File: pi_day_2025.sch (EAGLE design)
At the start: 109 parts, among them IC1 W25Q64JVXGIQ, J4 SM03B-SRSS-TB(LF)(SN), Q2 310mA/60V/1.6Ω, U1 APS6404L-3SQR-ZR, U2 RP2350A, U3 TPS76318DBVRG4, U4 TPS63001DRCR, U5 TXS0108EPWRG4, U6 LSM6DS3TR-C, U7 MCP73833T-AMI/MF, U8 TPS2113APWR, U9 ESP32-C3-MINI-1-N4, Y1 12MHz

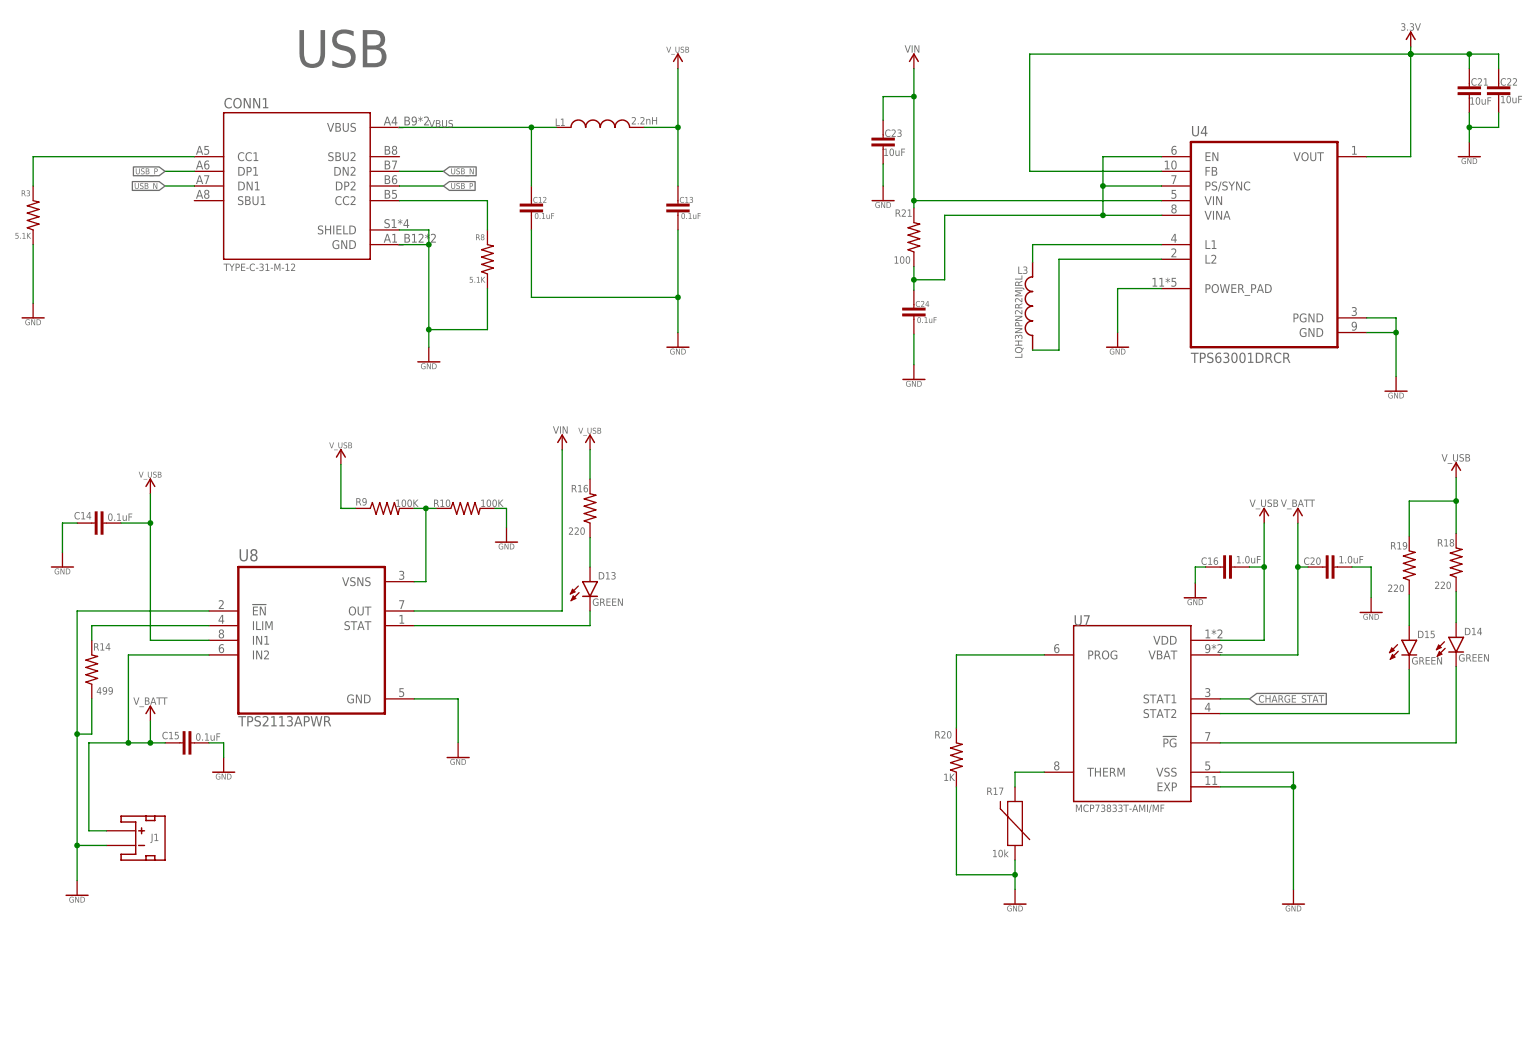
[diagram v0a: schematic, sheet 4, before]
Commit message: Added voltage symbols
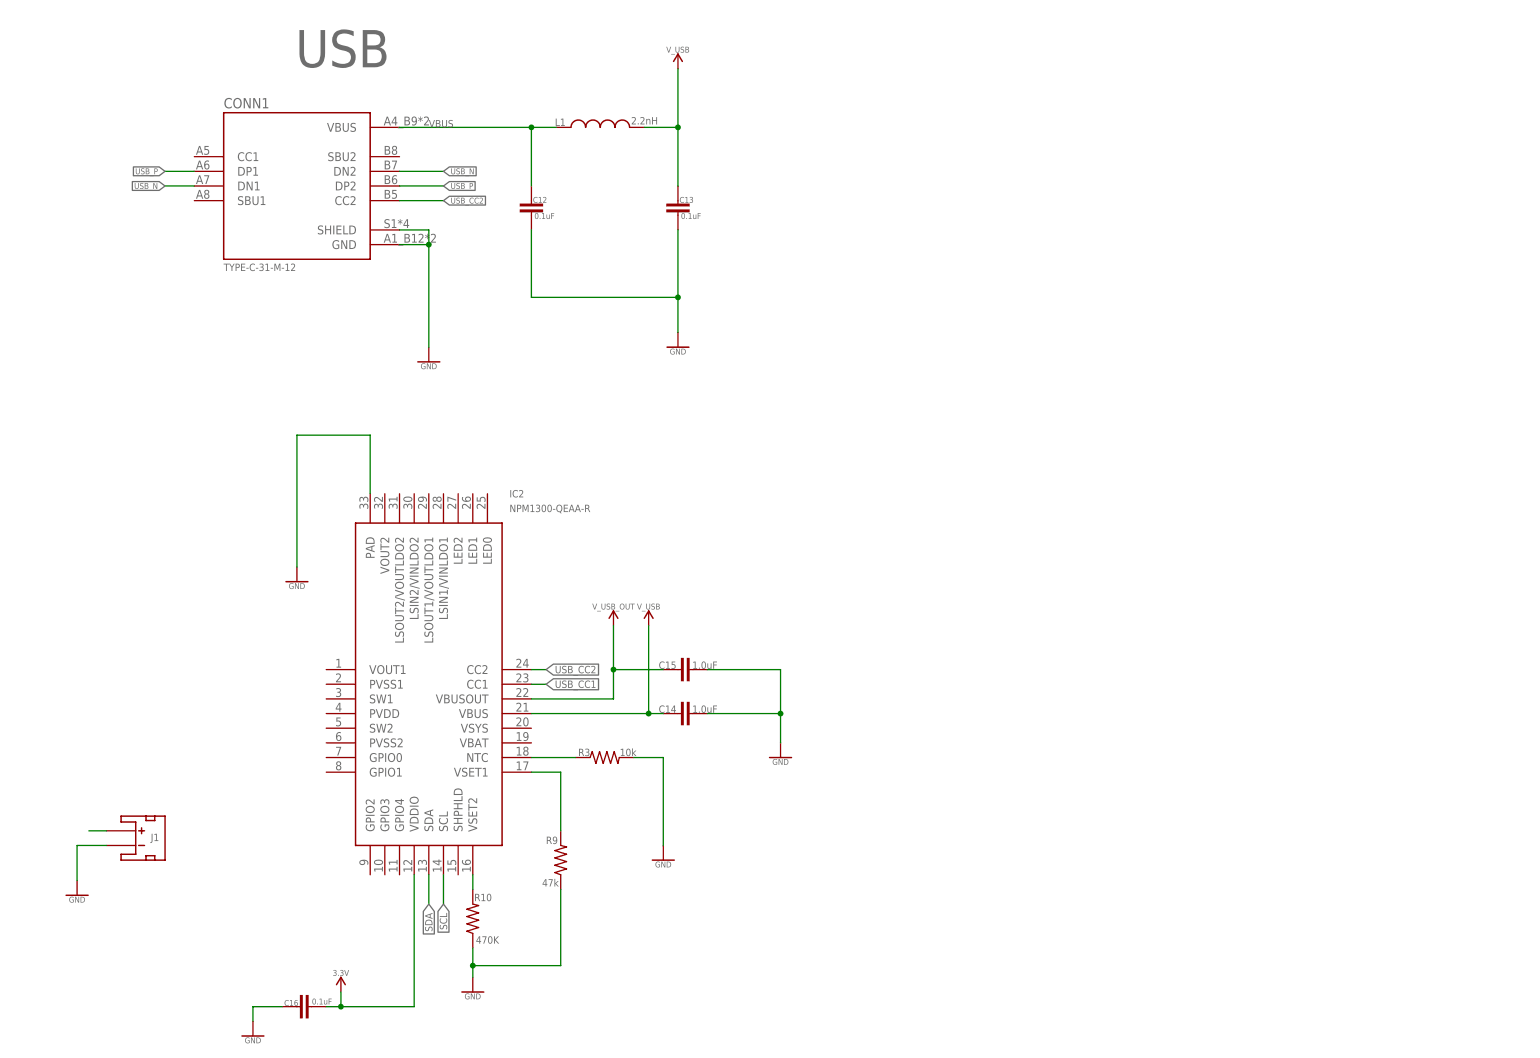
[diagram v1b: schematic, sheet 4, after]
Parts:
- removed C20, C26: 1.0uF, SparkFun-Capacitors:1.0UF-0402-16V-10%
- removed C21, C22, C23: 10uF, SparkFun-Capacitors:10UF-0402T-6.3V-20%
- removed C24: 0.1uF, SparkFun-Capacitors:0.1UF-0402-16V-10%
- removed C25: 4.7uF, SparkFun-Capacitors:4.7UF-0402_TIGHT-6.3V-20%-X5R
- removed D13, D14, D15: GREEN, SparkFun-LED:LED-GREEN0603
- removed L3: LQH3NPN2R2MJRL, LQH3NPN2R2MJRL:LQH3NPN2R2MJRL
- removed R14: 499, SparkFun-Resistors:RESISTOR0402
- removed R16, R18, R19: 220, SparkFun-Resistors:220OHM-0402-TIGHT-1/16W-1%
- removed R17: 10k, SparkFun-Resistors:NTC-THERMISTOR-0603
- removed R20: 1K, SparkFun-Resistors:1KOHM-0402-1/16W-1%
- removed R21: 100, SparkFun-Resistors:100OHM-0402-TIGHT-1/16W-1%
- removed R8: 5.1K, SparkFun-Resistors:RESISTOR0402
- removed U3: TPS76318DBVRG4, TPS76318DBVRG4:TPS76318DBVRG4
- removed U4: TPS63001DRCR, TPS63001DRCR:TPS63001DRCR
- removed U7: MCP73833T-AMI/MF, MCP73833T-AMI_MF:MCP73833T-AMI/MF
- removed U8: TPS2113APWR, TPS2113APWR:TPS2113APWR
- added IC2: NPM1300-QEAA-R, SamacSys_Parts:NPM1300-QEAA-R
- C14, C15: value 0.1uF -> 1.0uF; device SparkFun-Capacitors:0.1UF-0402-10V-10%-X7R -> SparkFun-Capacitors:1.0UF-0402-16V-10%
- C16: value 1.0uF -> 0.1uF; device SparkFun-Capacitors:1.0UF-0402-16V-10% -> SparkFun-Capacitors:0.1UF-0402-16V-10%
- R10: value 100K -> 470K; device SparkFun-Resistors:100KOHM-0402-1/16W-1% -> SparkFun-Resistors:RESISTOR0402
- R3: value 5.1K -> 10k; device SparkFun-Resistors:RESISTOR0402 -> SparkFun-Resistors:10KOHM-0402-1/16W-1%
- R4: value DNF -> (none)
- R5: value 1K -> (none)
- R6, R7: value 2.2K -> (none)
- R9: value 100K -> 47k; device SparkFun-Resistors:100KOHM-0402-1/16W-1% -> SparkFun-Resistors:47KOHM-0402-1/10W-1%
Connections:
- removed net N$10: D13.C, U8.STAT
- removed net N$14: R17.2, U7.THERM
- removed net N$15: D14.A, R18.1
- removed net N$16: D14.C, U7.!PG
- removed net N$17: D15.A, R19.1
- removed net N$18: D15.C, U7.STAT2
- removed net N$19: R20.2, U7.PROG
- removed net N$20: L3.P$2, U4.L1
- removed net N$21: L3.P$1, U4.L2
- removed net N$22: C24.1, R21.1, U4.EN, U4.PS/SYNC, U4.VINA
- removed net N$8: R14.2, U8.ILIM
- removed net N$9: D13.A, R16.1
- removed net VIN: C23.1, R21.2, U4.VIN, U8.OUT
- removed net V_BATT: C15.1, C20.1, J1.+, U7.VBAT, U8.IN2
- new net N$38: J1.+
- new net USB_CC1: IC2.CC1
- new net USB_CC2: CONN1.CC2, IC2.CC2
- net 1.8V: no longer C25.1, U3.OUT
- net 3.3V: now also C16.2, IC2.VDDIO; no longer C21.1, C22.1, C26.1, U3.EN, U3.IN, U4.FB, U4.VOUT
- net CHARGE_STAT: no longer U7.STAT1
- net GND: now also C14.2, IC2.PAD, R10.1, R3.2, R9.1; no longer C14.1, C20.2, C21.2, C22.2, C23.2, C24.2, C25.2, C26.2, R10.2, R14.1, R17.1, R20.1, R3.1, R8.1, U3.GND, U4.GND, U4.PGND, U4.POWER_PAD, U7.EXP, U7.VSS, U8.!EN, U8.GND
- net N$3: now also IC2.NTC, R3.1; no longer CONN1.CC1, R3.2
- net N$6: now also IC2.VSET2, R10.2; no longer R10.1, R9.2, U8.VSNS
- net N$7: now also IC2.VSET1, R9.2; no longer CONN1.CC2, R8.2
- net SCL: now also IC2.SCL
- net SDA: now also IC2.SDA
- net V_USB: now also C14.1, C15.1, IC2.VBUS, IC2.VBUSOUT; no longer C14.2, C16.2, R16.2, R18.2, R19.2, R9.1, U7.VDD, U8.IN1
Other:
- moved on the sheet: C14, C15, C16, R10, R3, R9

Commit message: more modification
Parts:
- added R8: 0, SparkFun-Resistors:0OHM-0603-1/10W
- R10: value 470K -> (none)
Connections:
- new net N$8: IC2.SHPHLD, R8.2
- net GND: now also R8.1
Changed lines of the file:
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@@
 <part name="GND22" library="SparkFun-PowerSymbols" library_urn="urn:adsk.eagle:library:530" deviceset="GND" device=""/>
 <part name="R9" library="SparkFun-Resistors" library_urn="urn:adsk.eagle:library:532" deviceset="47KOHM" device="-0402-1/10W-1%" package3d_urn="urn:adsk.eagle:package:41389023/1" value="47k"/>
-<part name="R10" library="SparkFun-Resistors" library_urn="urn:adsk.eagle:library:532" deviceset="RESISTOR" device="0402" package3d_urn="urn:adsk.eagle:package:39657/2" value="470K"/>
+<part name="R10" library="SparkFun-Resistors" library_urn="urn:adsk.eagle:library:532" deviceset="RESISTOR" device="0402" package3d_urn="urn:adsk.eagle:package:39657/2" value=" "/>
 <part name="C14" library="SparkFun-Capacitors" library_urn="urn:adsk.eagle:library:510" deviceset="1.0UF" device="-0402-16V-10%" package3d_urn="urn:adsk.eagle:package:41385089/1" value="1.0uF"/>
 <part name="GND23" library="SparkFun-PowerSymbols" library_urn="urn:adsk.eagle:library:530" deviceset="GND" device=""/>
@@
 <part name="C16" library="SparkFun-Capacitors" library_urn="urn:adsk.eagle:library:510" deviceset="0.1UF" device="-0402-16V-10%" package3d_urn="urn:adsk.eagle:package:41385089/1" override_package3d_urn="urn:adsk.eagle:package:44163394/2" override_package_urn="urn:adsk.eagle:footprint:37389/1" override_locally_modified="yes" value="0.1uF"/>
 <part name="GND26" library="SparkFun-PowerSymbols" library_urn="urn:adsk.eagle:library:530" deviceset="GND" device=""/>
+<part name="R8" library="SparkFun-Resistors" library_urn="urn:adsk.eagle:library:532" deviceset="0OHM" device="-0603-1/10W" package3d_urn="urn:adsk.eagle:package:41389018/1" value="0"/>
 </parts>
 <sheets>
@@
 <attribute name="VALUE" x="48.26" y="2.286" size="1.016" layer="96" font="vector" ratio="20" align="top-center"/>
 </instance>
+<instance part="R8" gate="G$1" x="83.82" y="22.098" smashed="yes" rot="R90">
+<attribute name="NAME" x="82.55" y="26.924" size="1.27" layer="95" font="vector" ratio="20" rot="R180" align="bottom-center"/>
+<attribute name="VALUE" x="83.058" y="17.272" size="1.27" layer="96" font="vector" ratio="20" rot="R180" align="top-center"/>
+</instance>
 </instances>
 <busses>
@@
 <junction x="86.36" y="14.732"/>
 <pinref part="R10" gate="G$1" pin="1"/>
+<pinref part="R8" gate="G$1" pin="1"/>
+<wire x1="83.82" y1="17.018" x2="83.82" y2="14.732" width="0.1524" layer="91"/>
+<wire x1="83.82" y1="14.732" x2="86.36" y2="14.732" width="0.1524" layer="91"/>
 </segment>
 <segment>
@@
 </segment>
 </net>
+<net name="N$8" class="0">
+<segment>
+<pinref part="R8" gate="G$1" pin="2"/>
+<pinref part="IC2" gate="G$1" pin="SHPHLD"/>
+<wire x1="83.82" y1="27.178" x2="83.82" y2="30.48" width="0.1524" layer="91"/>
+</segment>
+</net>

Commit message: update
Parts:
- added S3: JS202011JCQN, JS202011JCQN:JS202011JCQN
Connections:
- new net N$9: S3.7
- new net V_BATT: IC2.VBAT, S3.6
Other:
- moved on the sheet: J1, R3
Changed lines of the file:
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@@
 <part name="GND26" library="SparkFun-PowerSymbols" library_urn="urn:adsk.eagle:library:530" deviceset="GND" device=""/>
 <part name="R8" library="SparkFun-Resistors" library_urn="urn:adsk.eagle:library:532" deviceset="0OHM" device="-0603-1/10W" package3d_urn="urn:adsk.eagle:package:41389018/1" value="0"/>
+<part name="S3" library="JS202011JCQN" deviceset="JS202011JCQN" device=""/>
+<part name="SUPPLY21" library="SparkFun-PowerSymbols_Sai" deviceset="V_BATT" device=""/>
+<part name="SUPPLY25" library="SparkFun-PowerSymbols_Sai" deviceset="V_BATT" device=""/>
 </parts>
 <sheets>
@@
 <attribute name="VALUE" x="121.92" y="121.666" size="1.016" layer="96" font="vector" ratio="20" align="top-center"/>
 </instance>
-<instance part="GND21" gate="1" x="17.78" y="26.924" smashed="yes">
-<attribute name="VALUE" x="17.78" y="26.67" size="1.016" layer="96" font="vector" ratio="20" align="top-center"/>
-</instance>
-<instance part="J1" gate="G$1" x="27.94" y="35.56" smashed="yes" rot="MR90">
-<attribute name="NAME" x="32.004" y="36.322" size="1.27" layer="95" font="vector" ratio="20" rot="MR0"/>
+<instance part="GND21" gate="1" x="251.46" y="24.384" smashed="yes">
+<attribute name="VALUE" x="251.46" y="24.13" size="1.016" layer="96" font="vector" ratio="20" align="top-center"/>
+</instance>
+<instance part="J1" gate="G$1" x="261.62" y="33.02" smashed="yes" rot="MR90">
+<attribute name="NAME" x="265.684" y="33.782" size="1.27" layer="95" font="vector" ratio="20" rot="MR0"/>
 </instance>
 <instance part="IC2" gate="G$1" x="60.96" y="66.04" smashed="yes">
@@
 <attribute name="VALUE" x="92.71" y="93.98" size="1.27" layer="96" font="vector" ratio="20" align="center-left"/>
 </instance>
-<instance part="R3" gate="G$1" x="109.22" y="50.8" smashed="yes">
-<attribute name="NAME" x="105.664" y="51.054" size="1.27" layer="95" font="vector" ratio="20" align="bottom-center"/>
-<attribute name="VALUE" x="113.284" y="52.324" size="1.27" layer="96" font="vector" ratio="20" align="top-center"/>
+<instance part="R3" gate="G$1" x="109.22" y="40.64" smashed="yes" rot="R270">
+<attribute name="NAME" x="109.474" y="44.196" size="1.27" layer="95" font="vector" ratio="20" rot="R270" align="bottom-center"/>
+<attribute name="VALUE" x="110.744" y="36.576" size="1.27" layer="96" font="vector" ratio="20" rot="R270" align="top-center"/>
 </instance>
 <instance part="GND6" gate="1" x="55.88" y="81.28" smashed="yes">
@@
 <attribute name="VALUE" x="116.84" y="76.454" size="1.016" layer="96" font="vector" ratio="20" align="bottom-center"/>
 </instance>
-<instance part="GND9" gate="1" x="119.38" y="33.02" smashed="yes">
-<attribute name="VALUE" x="119.38" y="32.766" size="1.016" layer="96" font="vector" ratio="20" align="top-center"/>
+<instance part="GND9" gate="1" x="109.22" y="17.78" smashed="yes">
+<attribute name="VALUE" x="109.22" y="17.526" size="1.016" layer="96" font="vector" ratio="20" align="top-center"/>
 </instance>
 <instance part="GND22" gate="1" x="86.36" y="10.16" smashed="yes">
@@
 <attribute name="NAME" x="82.55" y="26.924" size="1.27" layer="95" font="vector" ratio="20" rot="R180" align="bottom-center"/>
 <attribute name="VALUE" x="83.058" y="17.272" size="1.27" layer="96" font="vector" ratio="20" rot="R180" align="top-center"/>
+</instance>
+<instance part="S3" gate="G$1" x="233.426" y="38.1" smashed="yes">
+<attribute name="NAME" x="225.806" y="44.45" size="1.27" layer="95" font="vector" ratio="20"/>
+<attribute name="VALUE" x="225.806" y="31.75" size="1.27" layer="96" font="vector" ratio="20" align="top-left"/>
+</instance>
+<instance part="SUPPLY21" gate="G$1" x="254" y="43.18" smashed="yes">
+<attribute name="VALUE" x="254" y="45.974" size="1.27" layer="96" font="vector" ratio="20" align="bottom-center"/>
+</instance>
+<instance part="SUPPLY25" gate="G$1" x="121.92" y="53.34" smashed="yes" rot="R270">
+<attribute name="VALUE" x="124.714" y="53.34" size="1.27" layer="96" font="vector" ratio="20" rot="R270" align="bottom-center"/>
 </instance>
 </instances>
@@
 <segment>
 <pinref part="J1" gate="G$1" pin="-"/>
-<wire x1="22.86" y1="35.56" x2="17.78" y2="35.56" width="0.1524" layer="91"/>
+<wire x1="256.54" y1="33.02" x2="251.46" y2="33.02" width="0.1524" layer="91"/>
 <pinref part="GND21" gate="1" pin="GND"/>
-<wire x1="17.78" y1="29.464" x2="17.78" y2="35.56" width="0.1524" layer="91"/>
+<wire x1="251.46" y1="26.924" x2="251.46" y2="33.02" width="0.1524" layer="91"/>
 </segment>
 <segment>
@@
 <pinref part="GND9" gate="1" pin="GND"/>
 <pinref part="R3" gate="G$1" pin="2"/>
-<wire x1="119.38" y1="35.56" x2="119.38" y2="50.8" width="0.1524" layer="91"/>
-<wire x1="119.38" y1="50.8" x2="114.3" y2="50.8" width="0.1524" layer="91"/>
+<wire x1="109.22" y1="20.32" x2="109.22" y2="35.56" width="0.1524" layer="91"/>
 </segment>
 <segment>
@@
 <segment>
 <pinref part="J1" gate="G$1" pin="+"/>
-<wire x1="22.86" y1="38.1" x2="19.812" y2="38.1" width="0.1524" layer="91"/>
+<wire x1="256.54" y1="35.56" x2="253.492" y2="35.56" width="0.1524" layer="91"/>
 </segment>
 </net>
@@
 <pinref part="R3" gate="G$1" pin="1"/>
 <pinref part="IC2" gate="G$1" pin="NTC"/>
-<wire x1="104.14" y1="50.8" x2="96.52" y2="50.8" width="0.1524" layer="91"/>
+<wire x1="109.22" y1="45.72" x2="109.22" y2="50.8" width="0.1524" layer="91"/>
+<wire x1="109.22" y1="50.8" x2="96.52" y2="50.8" width="0.1524" layer="91"/>
 </segment>
 </net>
@@
 </segment>
 </net>
+<net name="N$9" class="0">
+<segment>
+<pinref part="S3" gate="G$1" pin="7"/>
+<wire x1="253.746" y1="35.306" x2="253.746" y2="35.56" width="0.1524" layer="91"/>
+<wire x1="253.746" y1="35.56" x2="246.126" y2="35.56" width="0.1524" layer="91"/>
+</segment>
+</net>
+<net name="V_BATT" class="0">
+<segment>
+<pinref part="S3" gate="G$1" pin="6"/>
+<pinref part="SUPPLY21" gate="G$1" pin="V_BATT"/>
+<wire x1="246.126" y1="38.1" x2="254" y2="38.1" width="0.1524" layer="91"/>
+<wire x1="254" y1="38.1" x2="254" y2="43.18" width="0.1524" layer="91"/>
+</segment>
+<segment>
+<pinref part="IC2" gate="G$1" pin="VBAT"/>
+<pinref part="SUPPLY25" gate="G$1" pin="V_BATT"/>
+<wire x1="96.52" y1="53.34" x2="121.92" y2="53.34" width="0.1524" layer="91"/>
+</segment>
+</net>
